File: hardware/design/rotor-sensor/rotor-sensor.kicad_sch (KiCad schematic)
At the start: 93 parts, among them J2 Conn_01x06, J517 Conn_ARM_JTAG_SWD_10, U1 MCP2021A-xxxE/SN, U2 AP22804AW5, U5 AP22804AW5, U500 ATSAMD21E18A-A, U501 AP2127K-ADJTRG1, U600 BMI088, Y508 ABS07-32.768KHZ-7-T

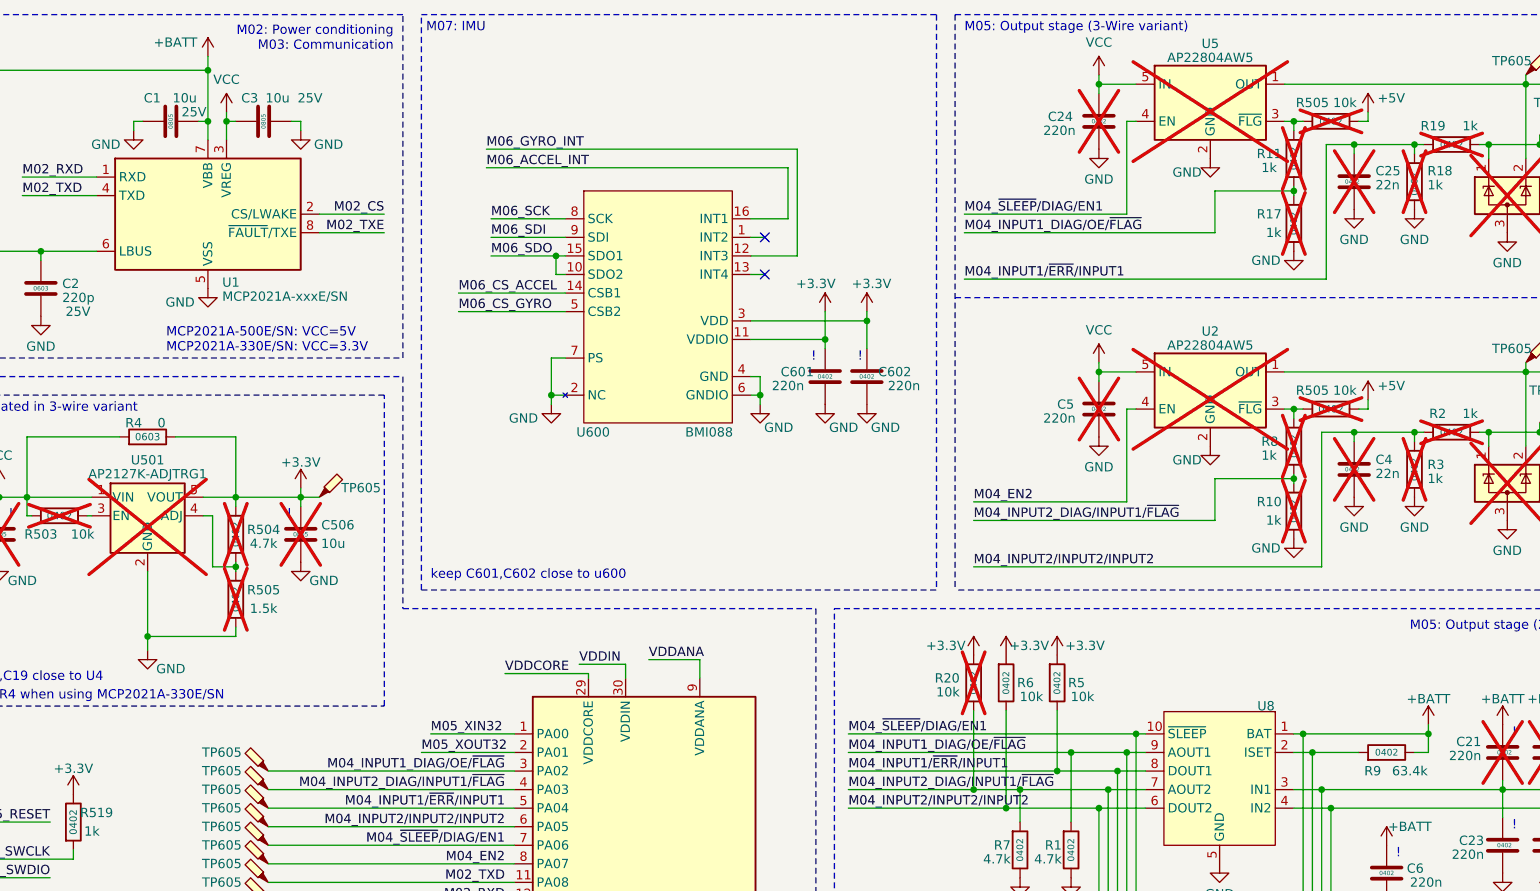
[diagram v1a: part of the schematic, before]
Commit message: 5V rail renamed to VCC Fixed size information on some resistors
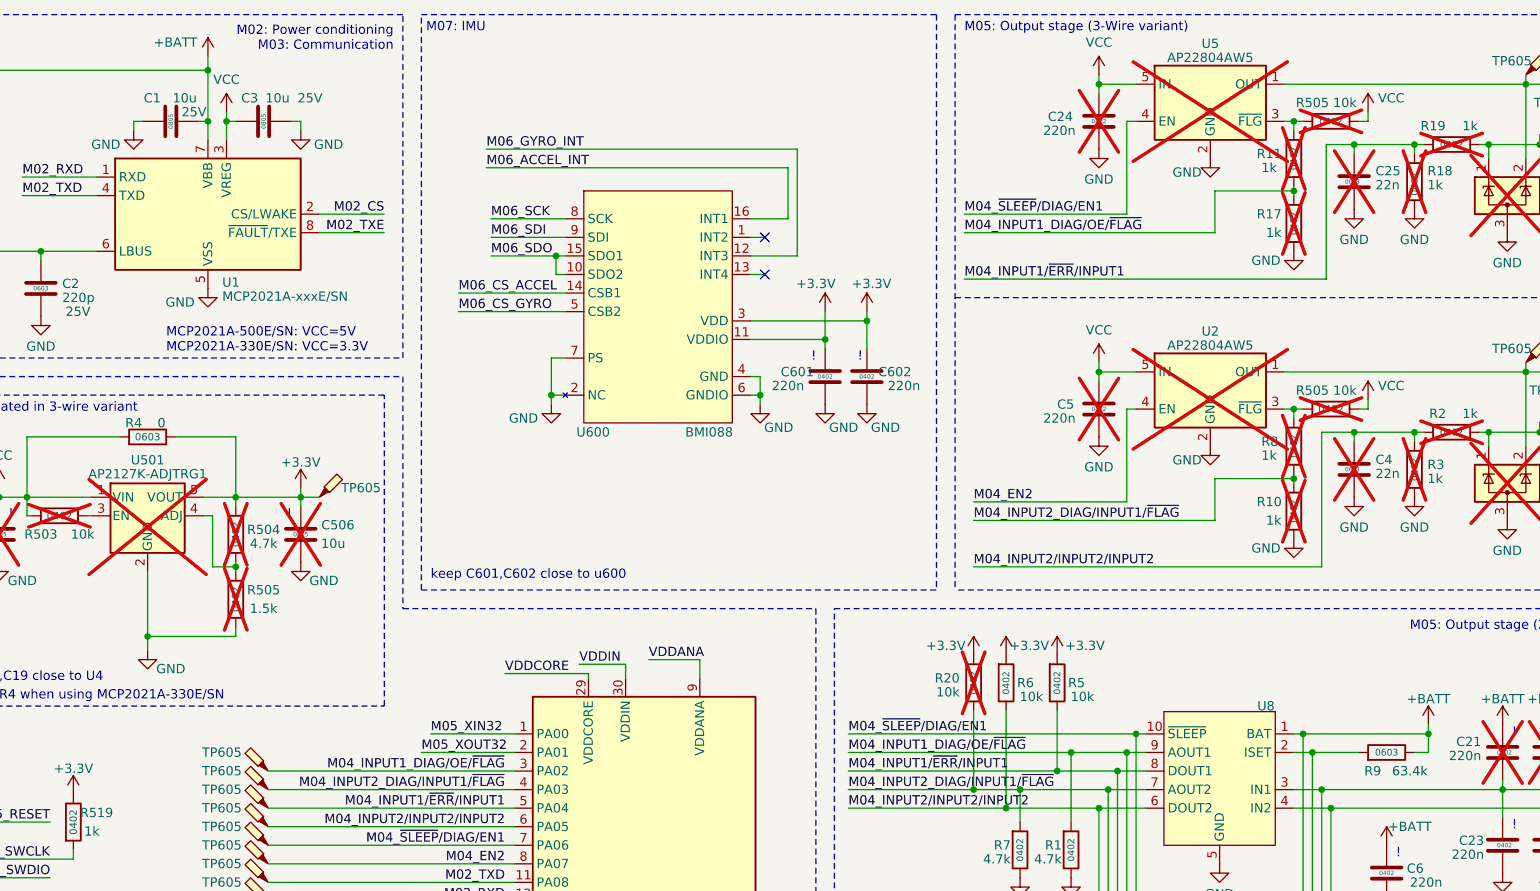
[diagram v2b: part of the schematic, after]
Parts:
- C25, C4, R9: Size 0402 -> 0603
- R4: SIze 0603 -> (none); Size (none) -> 0603
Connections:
- net +5V is gone; now on net VCC: R505.1, R505.1
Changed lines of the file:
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@@
       (effects (font (size 1.27 1.27)) hide)
     )
-    (property "Size" "0402" (at 308.61 104.14 0)
+    (property "Size" "0603" (at 308.61 104.14 0)
       (effects (font (size 0.5842 0.5842)) (justify right))
     )
@@
     )
   )
+  (symbol (lib_id "power:VCC") (at 311.785 94.615 0) (unit 1)
+    (in_bom yes) (on_board yes) (dnp no)
+    (property "Reference" "#PWR048" (at 311.785 98.425 0)
+      (effects (font (size 1.27 1.27)) hide)
+    )
+    (property "Value" "VCC" (at 314.96 92.71 0)
+      (effects (font (size 1.27 1.27)))
+    )
+    (property "Footprint" "" (at 311.785 94.615 0)
+      (effects (font (size 1.27 1.27)) hide)
+    )
+    (property "Datasheet" "" (at 311.785 94.615 0)
+      (effects (font (size 1.27 1.27)) hide)
+    )
+    (pin "1")
+    (instances
+      (project "rotor-sensor"
+        (path "/d35462db-b405-4e6b-820c-984876fa429d"
+          (reference "#PWR048") (unit 1)
+        )
+      )
+    )
+  )
   (symbol (lib_id "power:GND") (at 124.46 116.84 0) (unit 1)
     (in_bom yes) (on_board yes) (dnp no)
@@
     )
   )
+  (symbol (lib_id "power:VCC") (at 311.785 55.245 0) (unit 1)
+    (in_bom yes) (on_board yes) (dnp no)
+    (property "Reference" "#PWR057" (at 311.785 59.055 0)
+      (effects (font (size 1.27 1.27)) hide)
+    )
+    (property "Value" "VCC" (at 314.96 53.34 0)
+      (effects (font (size 1.27 1.27)))
+    )
+    (property "Footprint" "" (at 311.785 55.245 0)
+      (effects (font (size 1.27 1.27)) hide)
+    )
+    (property "Datasheet" "" (at 311.785 55.245 0)
+      (effects (font (size 1.27 1.27)) hide)
+    )
+    (pin "1")
+    (instances
+      (project "rotor-sensor"
+        (path "/d35462db-b405-4e6b-820c-984876fa429d"
+          (reference "#PWR057") (unit 1)
+        )
+      )
+    )
+  )
   (symbol (lib_id "power:+3.3V") (at 262.255 129.54 0) (unit 1)
     (in_bom yes) (on_board yes) (dnp no)
@@
       (effects (font (size 1.27 1.27)) hide)
     )
-    (property "Size" "0402" (at 308.61 64.77 0)
+    (property "Size" "0603" (at 308.61 64.77 0)
       (effects (font (size 0.5842 0.5842)) (justify right))
     )
@@
       (effects (font (size 1.27 1.27)) hide)
     )
-    (property "SIze" "0603" (at 144.78 99.695 90)
-      (effects (font (size 0.9906 0.9906)))
+    (property "Size" "0603" (at 144.78 99.695 90)
+      (effects (font (size 1 1)))
     )
     (pin "1")
@@
     )
   )
-  (symbol (lib_id "power:+5V") (at 311.785 94.615 0) (unit 1)
-    (in_bom yes) (on_board yes) (dnp no)
-    (property "Reference" "#PWR067" (at 311.785 98.425 0)
-      (effects (font (size 1.27 1.27)) hide)
-    )
-    (property "Value" "+5V" (at 314.96 92.71 0)
-      (effects (font (size 1.27 1.27)))
-    )
-    (property "Footprint" "" (at 311.785 94.615 0)
-      (effects (font (size 1.27 1.27)) hide)
-    )
-    (property "Datasheet" "" (at 311.785 94.615 0)
-      (effects (font (size 1.27 1.27)) hide)
-    )
-    (pin "1")
-    (instances
-      (project "rotor-sensor"
-        (path "/d35462db-b405-4e6b-820c-984876fa429d"
-          (reference "#PWR067") (unit 1)
-        )
-      )
-    )
-  )
-  (symbol (lib_id "power:+5V") (at 311.785 55.245 0) (unit 1)
-    (in_bom yes) (on_board yes) (dnp no)
-    (property "Reference" "#PWR066" (at 311.785 59.055 0)
-      (effects (font (size 1.27 1.27)) hide)
-    )
-    (property "Value" "+5V" (at 314.96 53.34 0)
-      (effects (font (size 1.27 1.27)))
-    )
-    (property "Footprint" "" (at 311.785 55.245 0)
-      (effects (font (size 1.27 1.27)) hide)
-    )
-    (property "Datasheet" "" (at 311.785 55.245 0)
-      (effects (font (size 1.27 1.27)) hide)
-    )
-    (pin "1")
-    (instances
-      (project "rotor-sensor"
-        (path "/d35462db-b405-4e6b-820c-984876fa429d"
-          (reference "#PWR066") (unit 1)
-        )
-      )
-    )
-  )
   (symbol (lib_id "power:GND") (at 142.875 57.785 0) (unit 1)
     (in_bom yes) (on_board yes) (dnp no)
@@
       (effects (font (size 1.27 1.27)) hide)
     )
-    (property "Size" "0402" (at 314.325 142.875 90)
+    (property "Size" "0603" (at 314.325 142.875 90)
       (effects (font (size 0.9144 0.9144)))
     )

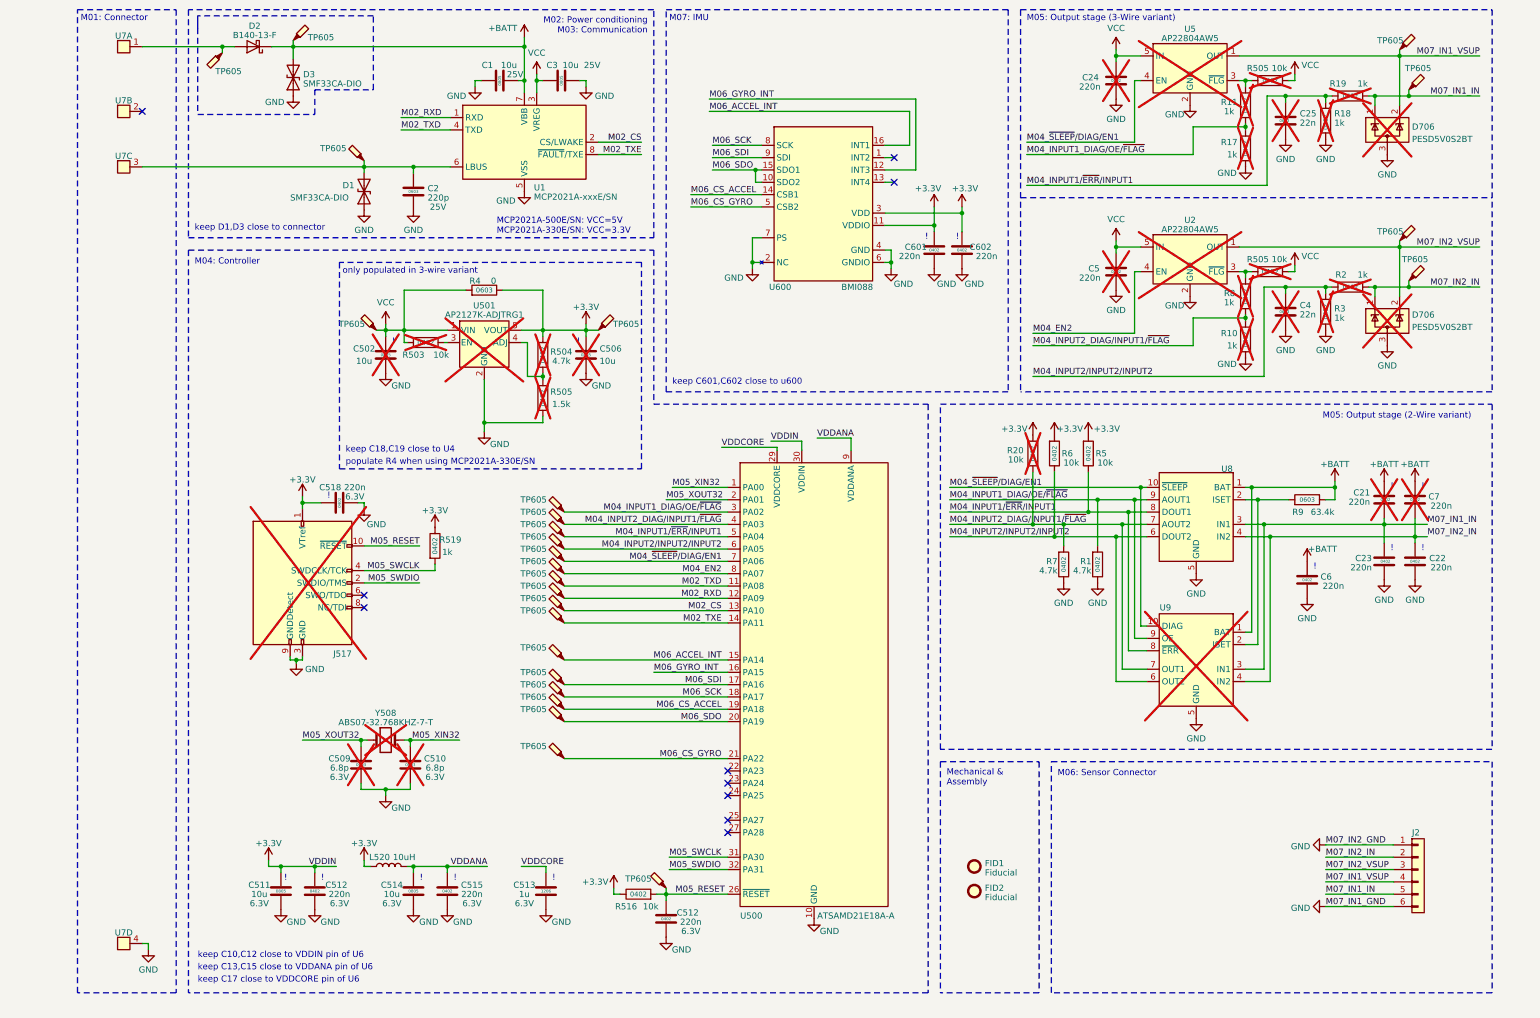
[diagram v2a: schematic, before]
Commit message: Gen2.1 final hardware design (#16)
* New schematic done

Works with TLIN1028-Q1 transceiver
Added BMP581 pressure sensor
Removed 3wire output stage

* FInal ordered hardware

New 3pin connector
Extra 2pin connector for cadence measurement
No 3pin sensor variant
DC/DC converter for MCU
Pressure sensor
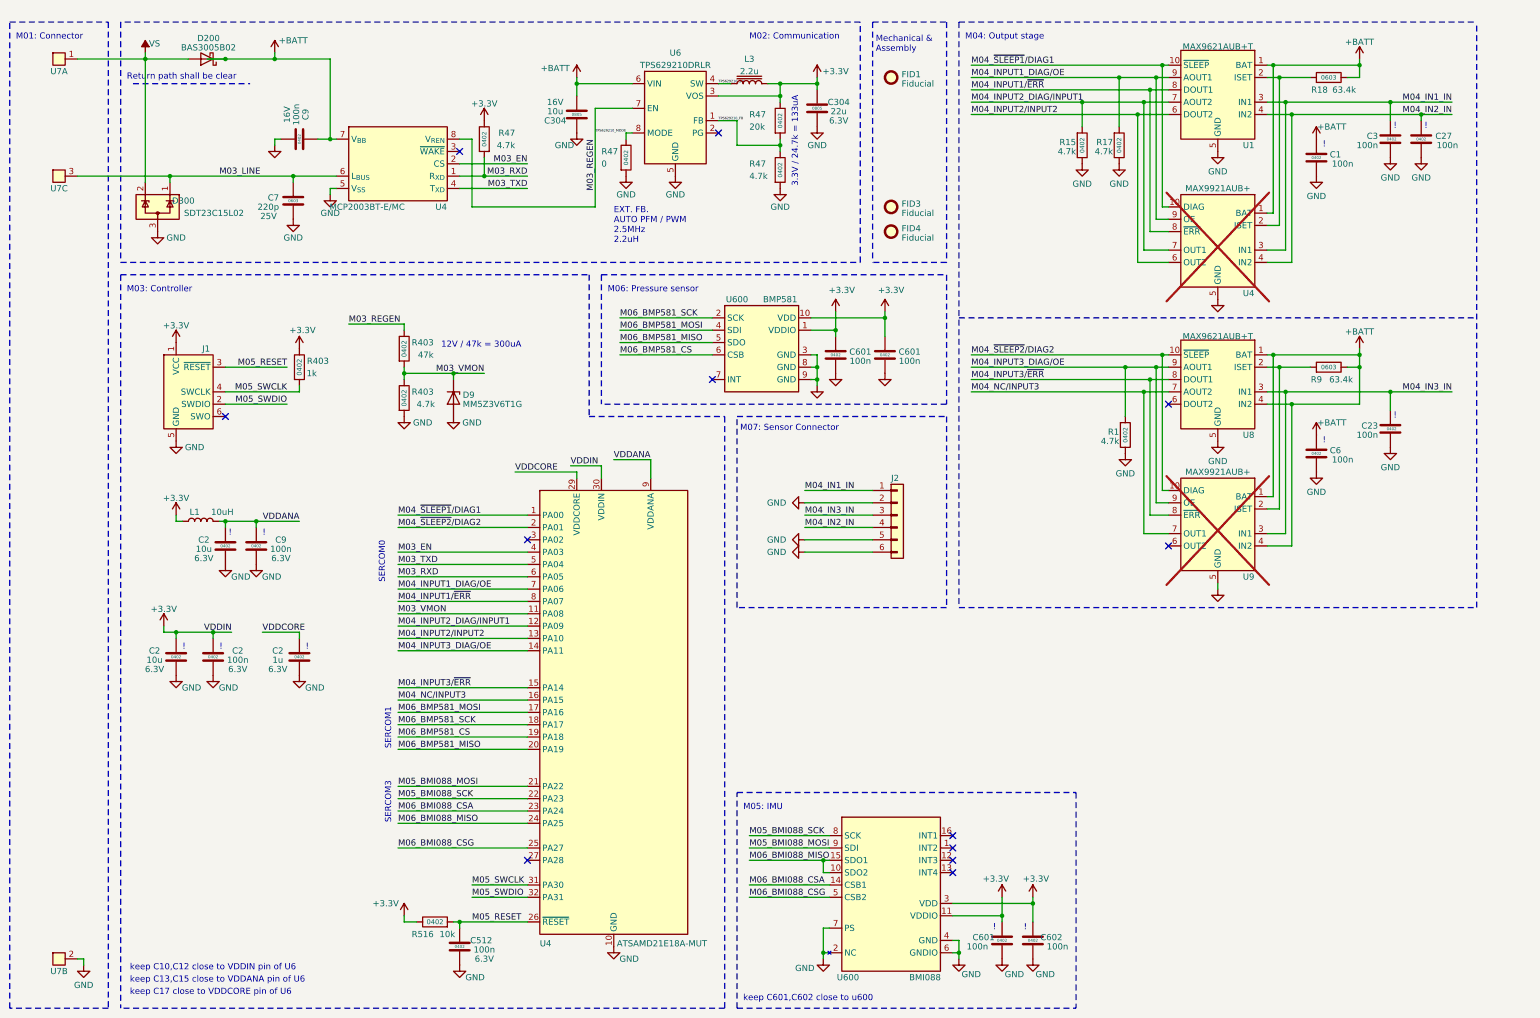
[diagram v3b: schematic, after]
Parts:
- removed C2: 220p, Capacitor_SMD:C_0603_1608Metric, symbol Device:C
- removed C21, C22, C24, C5, C512, C515, C518: 220n, Capacitor_SMD:C_0402_1005Metric, symbol Device:C
- removed C25, C4: 22n, Capacitor_SMD:C_0603_1608Metric, symbol Device:C
- removed C502, C506, C511, C514: 10u, Capacitor_SMD:C_0805_2012Metric, symbol Device:C
- removed C509, C510: 6.8p, Capacitor_SMD:C_0603_1608Metric, symbol Device:C
- removed C513: 1u, Capacitor_SMD:C_1206_3216Metric, symbol Device:C
- removed D1, D3: SMF33CA-DIO, Diode_SMD:D_SMF, symbol Device:D_TVS
- removed D2: B140-13-F, Diode_SMD:D_SMA, symbol Device:D_Schottky
- removed D706 (x2): PESD5V0S2BT, Package_TO_SOT_SMD:SOT-23, symbol Power_Protection:SP0502BAHT
- removed FID2: Fiducial, Fiducial:Fiducial_0.5mm_Mask1mm, symbol Mechanical:Fiducial
- removed J517: Conn_ARM_JTAG_SWD_10, Connector_PinHeader_1.27mm:PinHeader_2x05_P1.27mm_Vertical_SMD, symbol Connector:Conn_ARM_JTAG_SWD_10
- removed L520: 10uH, Inductor_SMD:L_0805_2012Metric, symbol Device:L
- removed R10, R11, R19, R2, R3, R519, R8: 1k, Resistor_SMD:R_0402_1005Metric, symbol Device:R
- removed R20, R5, R503, R505 (x2), R6: 10k, Resistor_SMD:R_0402_1005Metric, symbol Device:R
- removed R4: 0, Resistor_SMD:R_0603_1608Metric, symbol Device:R
- removed R504, R7: 4.7k, Resistor_SMD:R_0402_1005Metric, symbol Device:R
- removed R505: 1.5k, Resistor_SMD:R_0402_1005Metric, symbol Device:R
- removed TP605: O4, TestPoint:TestPoint_Pad_1.0x1.0mm, symbol Connector:TestPoint_Probe
- removed TP605: P1, TestPoint:TestPoint_Pad_1.0x1.0mm, symbol Connector:TestPoint_Probe
- removed TP605: O6, TestPoint:TestPoint_Pad_1.0x1.0mm, symbol Connector:TestPoint_Probe
- removed TP605: M1, TestPoint:TestPoint_Pad_1.0x1.0mm, symbol Connector:TestPoint_Probe
- removed TP605: S4, TestPoint:TestPoint_Pad_1.0x1.0mm, symbol Connector:TestPoint_Probe
- removed TP605: B1, TestPoint:TestPoint_Pad_1.0x1.0mm, symbol Connector:TestPoint_Probe
- removed TP605: O3, TestPoint:TestPoint_Pad_1.0x1.0mm, symbol Connector:TestPoint_Probe
- removed TP605: V1, TestPoint:TestPoint_Pad_1.0x1.0mm, symbol Connector:TestPoint_Probe
- removed TP605: O7, TestPoint:TestPoint_Pad_1.0x1.0mm, symbol Connector:TestPoint_Probe
- removed TP605: O8, TestPoint:TestPoint_Pad_1.0x1.0mm, symbol Connector:TestPoint_Probe
- removed TP605: O2, TestPoint:TestPoint_Pad_1.0x1.0mm, symbol Connector:TestPoint_Probe
- removed TP605: S7, TestPoint:TestPoint_Pad_1.0x1.0mm, symbol Connector:TestPoint_Probe
- removed TP605: S1, TestPoint:TestPoint_Pad_1.0x1.0mm, symbol Connector:TestPoint_Probe
- removed TP605: B3, TestPoint:TestPoint_Pad_1.0x1.0mm, symbol Connector:TestPoint_Probe
- removed TP605: O10, TestPoint:TestPoint_Pad_1.0x1.0mm, symbol Connector:TestPoint_Probe
- removed TP605: S6, TestPoint:TestPoint_Pad_1.0x1.0mm, symbol Connector:TestPoint_Probe
- removed TP605: P2, TestPoint:TestPoint_Pad_1.0x1.0mm, symbol Connector:TestPoint_Probe
- removed TP605: O5, TestPoint:TestPoint_Pad_1.0x1.0mm, symbol Connector:TestPoint_Probe
- removed TP605: S5, TestPoint:TestPoint_Pad_1.0x1.0mm, symbol Connector:TestPoint_Probe
- removed TP605: B2, TestPoint:TestPoint_Pad_1.0x1.0mm, symbol Connector:TestPoint_Probe
- removed TP605: B5, TestPoint:TestPoint_Pad_1.0x1.0mm, symbol Connector:TestPoint_Probe
- removed TP605: S3, TestPoint:TestPoint_Pad_1.0x1.0mm, symbol Connector:TestPoint_Probe
- removed TP605: B4, TestPoint:TestPoint_Pad_1.0x1.0mm, symbol Connector:TestPoint_Probe
- removed TP605: O1, TestPoint:TestPoint_Pad_1.0x1.0mm, symbol Connector:TestPoint_Probe
- removed TP605: V2, TestPoint:TestPoint_Pad_1.0x1.0mm, symbol Connector:TestPoint_Probe
- removed TP605: O9, TestPoint:TestPoint_Pad_1.0x1.0mm, symbol Connector:TestPoint_Probe
- removed U1: MCP2021A-xxxE/SN, Package_SO:SOIC-8_3.9x4.9mm_P1.27mm, symbol Interface_CAN_LIN:MCP2021A-xxxxSN
- removed U2, U5: AP22804AW5, Package_TO_SOT_SMD:SOT-23-5, symbol Power_Management:AP22804AW5
- removed U500: ATSAMD21E18A-A, Package_QFP:TQFP-32_7x7mm_P0.8mm, symbol MCU_Microchip_SAMD:ATSAMD21E18A-A
- removed U501: AP2127K-ADJTRG1, Package_TO_SOT_SMD:SOT-23-5, symbol Regulator_Linear:AP2127K-ADJ
- removed unit 4 of U7
- removed Y508: ABS07-32.768KHZ-7-T, Crystal:Crystal_SMD_3215-2Pin_3.2x1.5mm, symbol Device:Crystal
- added C2 (x2): 10u, Capacitor_SMD:C_0402_1005Metric, symbol Device:C
- added C2, C27, C601 (x2), C9 (x2): 100n, Capacitor_SMD:C_0402_1005Metric, symbol Device:C
- added C2: 1u, Capacitor_SMD:C_0402_1005Metric, symbol Device:C
- added C304: 22u, Capacitor_SMD:C_0805_2012Metric, symbol Device:C
- added C304: 10u, Capacitor_SMD:C_0805_2012Metric, symbol Device:C
- added D200: BAS3005B02, Diode_SMD:D_SOD-523, symbol Device:D_Schottky
- added D300: SDT23C15L02, Package_TO_SOT_SMD:SOT-23, symbol Power_Protection:SP0502BAHT
- added D9: MM5Z3V6T1G, Diode_SMD:D_SOD-523, symbol Device:D_Zener
- added FID3, FID4: Fiducial, Fiducial:Fiducial_0.5mm_Mask1mm, symbol Mechanical:Fiducial
- added J1: Conn_ARM_SWD_TagConnect_TC2030-NL, Connector:Tag-Connect_TC2030-IDC-NL_2x03_P1.27mm_Vertical, symbol Connector:Conn_ARM_SWD_TagConnect_TC2030-NL
- added L1: 10uH, Inductor_SMD:L_0603_1608Metric, symbol Device:L
- added L3: 2.2u, Inductor_SMD:L_Coilcraft_LPS3010, symbol Device:L_Iron
- added R15, R403, R47 (x2): 4.7k, Resistor_SMD:R_0402_1005Metric, symbol Device:R
- added R403: 1k, Resistor_SMD:R_0402_1005Metric, symbol Device:R
- added R403: 47k, Resistor_SMD:R_0402_1005Metric, symbol Device:R
- added R47: 0, Resistor_SMD:R_0402_1005Metric, symbol Device:R
- added R47: 20k, Resistor_SMD:R_0402_1005Metric, symbol Device:R
- added U1: MAX9621AUB+T, Package_SO:MSOP-10_3x3mm_P0.5mm, symbol local_symbols:MAX9621
- added U4: ATSAMD21E18A-MUT, Package_DFN_QFN:VQFN-32-1EP_5x5mm_P0.5mm_EP3.5x3.5mm, symbol MCU_Microchip_SAMD:ATSAMD21E18A-A
- added U4: MAX9921AUB+, Package_SO:MSOP-10_3x3mm_P0.5mm, symbol local_symbols:MAX9921
- added U4: MCP2003BT-E/MC, Package_DFN_QFN:DFN-8-1EP_3x2mm_P0.5mm_EP1.7x1.4mm, symbol local:MCP2003
- added U6: TPS629210DRLR, Package_TO_SOT_SMD:SOT-583-8, symbol local_symbols:TPS629210
- added U600: BMP581, local_footprints:Bosch_LGA10, symbol local_symbols:BMP581
- C1, C3: value 10u -> 100n; footprint Capacitor_SMD:C_0805_2012Metric -> Capacitor_SMD:C_0402_1005Metric; Rating 25V -> (none); Size 0805 -> 0402
- C23, C512, C6, C601, C602: value 220n -> 100n
- C7: value 220n -> 220p; footprint Capacitor_SMD:C_0402_1005Metric -> Capacitor_SMD:C_0603_1608Metric; Rating (none) -> 25V; Size 0402 -> 0603; now fitted
- J2: footprint local_footprints:SMD_6PIN -> local_footprints:SOIC-6
- R17: value 1k -> 4.7k; now fitted
- R18: value 1k -> 63.4k; footprint Resistor_SMD:R_0402_1005Metric -> Resistor_SMD:R_0603_1608Metric; Size 0402 -> 0603; now fitted
- U7: footprint local_footprints:SMD_4PIN -> local_footprints:SOIC-4
- U8: value ~ -> MAX9621AUB+T
- U9: value ~ -> MAX9921AUB+
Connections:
- net M07_IN2_VSUP is gone; now on net M04_IN3_IN: J2.3 (Pin_3)
- net VCC is gone; now on net GND: C3.1
- net +3.3V: now also C2.2, C2.2, C304.1, C601.2, C601.2, J1.1 (VCC), L1.1, L3.2, R403.1, R47.1, R47.1, U4.30 (VDDIN), U6.3 (VOS), U600.1 (VDDIO), U600.10 (VDD)
- net +BATT: now also R18.1, U8.4 (IN2), U9.4 (IN2), C304.2, C9.2, D200.1 (K), U1.1 (BAT), U4.1 (BAT), U4.7 (V_{BB}), U6.6 (VIN); no longer C7.2
- net GND: now also C7.2, J2.2 (Pin_2), J2.5 (Pin_5), U7.2, C2.1, C2.1, C2.1, C2.1, C27.1, C304.1, C304.2, C601.1, C601.1, C9.1, C9.1, D300.3 (A), D9.2 (A), J1.5 (GND), R15.1, R403.2, R47.2, R47.2, U1.5 (GND), U4.10 (GND), U4.28 (GND), U4.33 (GND), U4.5 (GND), U4.5 (V_{SS}), U6.5 (GND), U600.3 (GND), U600.8 (GND), U600.9 (GND); no longer C3.2, J2.1 (Pin_1), R18.1
- net M05_RESET: now also J1.3 (~{RESET}), U4.26 (~{RESET})
- net M05_SWCLK: now also J1.4 (SWCLK), R403.2, U4.31 (PA30)
- net M05_SWDIO: now also J1.2 (SWDIO), U4.32 (PA31)
- net VDDANA: now also C2.2, C9.2, L1.2, U4.9 (VDDANA)
- net VDDCORE: now also C2.2, U4.29 (VDDCORE)
- net M03_LINE: now reaches U7.3
- net M03_LINE: now also C7.1, D300.1 (K), U4.6 (L_{BUS})
- net VS: now reaches U7.1
- net VS: now also D200.2 (A), D300.2 (K)
- net M04_INPUT1_DIAG/OE/~{FLAG} renamed M04_INPUT3_DIAG/OE
- net M04_INPUT3_DIAG/OE: now also U4.14 (PA11); no longer R17.2
- net M04_INPUT1/~{ERR}/INPUT1 renamed M04_INPUT3/~{ERR}
- net M04_INPUT3/~{ERR}: now also U4.15 (PA14); no longer R18.2
- net M04_INPUT2_DIAG/INPUT1/~{FLAG} renamed M04_NC/INPUT3
- net M04_NC/INPUT3: now also U4.16 (PA15)
- net M04_INPUT2/INPUT2/INPUT2: no longer names the net of U9.6 (OUT2)
- net M04_INPUT2/INPUT2/INPUT2: no longer U8.6 (DOUT2)
- net M04_~{SLEEP}/DIAG/EN1 renamed M04_~{SLEEP2}/DIAG2
- net M04_~{SLEEP2}/DIAG2: now also U4.2 (PA01)
- net M06_ACCEL_INT: no longer names the net of U600.16 (INT1)
- net M06_CS_ACCEL renamed M06_BMI088_CSA
- net M06_BMI088_CSA: now also U4.23 (PA24)
- net M06_CS_GYRO renamed M06_BMI088_CSG
- net M06_BMI088_CSG: now also U4.25 (PA27)
- net M06_GYRO_INT: no longer names the net of U600.12 (INT3)
- net M06_SCK renamed M05_BMI088_SCK
- net M05_BMI088_SCK: now also U4.22 (PA23)
- net M06_SDI renamed M05_BMI088_MOSI
- net M05_BMI088_MOSI: now also U4.21 (PA22)
- net M06_SDO renamed M06_BMI088_MISO
- net M06_BMI088_MISO: now also U4.24 (PA25)
- net M07_IN1_IN renamed M04_IN3_IN
- net M04_IN3_IN: no longer J2.5 (Pin_5)
- net M07_IN1_VSUP renamed M04_IN2_IN
- net M04_IN2_IN: now also C27.2, U1.4 (IN2), U4.4 (IN2)
- removed net M07_IN2_IN: C7.1, J2.2 (Pin_2), U8.4 (IN2), U9.4 (IN2)
- new net: R18.2, U1.2 (ISET), U4.2 (ISET)
- new net M03_EN: U4.2 (CS), U4.4 (PA03)
- new net M03_REGEN: R403.1, U4.8 (V_{REN}), U6.7 (EN)
- new net M03_RXD: R47.2, U4.1 (R_{XD}), U4.6 (PA05)
- new net M03_TXD: U4.4 (T_{XD}), U4.5 (PA04)
- new net M03_VMON: D9.1 (K), R403.1, R403.2, U4.11 (PA08)
- new net M04_IN1_IN: C3.2, J2.1 (Pin_1), U1.3 (IN1), U4.3 (IN1)
- new net M04_INPUT1_DIAG/OE: R17.2, U1.9 (AOUT1), U4.7 (PA06), U4.9 (OE)
- new net M04_INPUT1/~{ERR}: U1.8 (DOUT1), U4.8 (PA07), U4.8 (~{ERR})
- new net M04_INPUT2_DIAG/INPUT1: R15.2, U1.7 (AOUT2), U4.12 (PA09), U4.7 (OUT1)
- new net M04_INPUT2/INPUT2: U1.6 (DOUT2), U4.13 (PA10), U4.6 (OUT2)
- new net M04_~{SLEEP1}/DIAG1: U1.10 (~{SLEEP}), U4.1 (PA00), U4.10 (DIAG)
- new net M06_BMP581_CS: U4.19 (PA18), U600.6 (CSB)
- new net M06_BMP581_MISO: U4.20 (PA19), U600.5 (SDO)
- new net M06_BMP581_MOSI: U4.17 (PA16), U600.4 (SDI)
- new net M06_BMP581_SCK: U4.18 (PA17), U600.2 (SCK)
- new net TPS629210_FB: R47.1, R47.2, U6.1 (FB)
- new net TPS629210_MODE: R47.1, U6.8 (MODE)
- new net TPS629210_SW: L3.1, U6.4 (SW)
- no-connect marks 10 -> 12
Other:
- note added: "12V / 47k = 300uA"
- note added: "3.3V / 24.7k = 133uA"
- note added: "EXT. FB. AUTO PFM / PWM 2.5MHz 2.2uH"
- note added: "M02: Communication"
- note added: "M03: Controller"
- note added: "M04: Output stage"
- note added: "M05: IMU"
- note added: "M06: Pressure sensor"
- note added: "M07: Sensor Connector"
- note added: "Return path shall be clear"
- note added: "SERCOM0"
- note added: "SERCOM1"
- note added: "SERCOM3"
- note removed: "M02: Power conditioning M03: Communication"
- note removed: "M04: Controller"
- note removed: "M05: Output stage (2-Wire variant)"
- note removed: "M05: Output stage (3-Wire variant)"
- note removed: "M06: Sensor Connector"
- note removed: "M07: IMU"
- note removed: "MCP2021A-500E/SN: VCC=5V MCP2021A-330E/SN: VCC=3.3V"
- note removed: "keep C18,C19 close to U4"
- note removed: "keep D1,D3 close to connector"
- note removed: "only populated in 3-wire variant"
- note removed: "populate R4 when using MCP2021A-330E/SN"
- moved on the sheet: C23, C512, C6, C601, C602, FID1, J2, R1, R516, R9, U600, U7A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
